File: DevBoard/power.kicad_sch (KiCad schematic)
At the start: 31 parts, among them U201 INA190A5IDDFR, U202 INA190A1IDDFR, U203 TPS70950DBVR, U204 TPS62177DQCR

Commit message: Dev board: cost-down pass (about $113 -> $80 per board at 5 boards)
Swaps from docs/devboard/cost-down-2026-10-14.md, datasheet-checked:
- L401/L501 XAL7030 -> SMMS1040-2R2M (Isat 18 A, Irms 12 A, 9 mOhm)
- L402/L502 SRP5030T -> APS0530M3R3H (new footprint L_Coilank_APS0530)
- L201 SRN4018TA -> FNR4030S100MT
- U203 TPS70950 -> HT7550-1, C204/C205 10 uF per Holtek's basic circuit
- C431/C434/C435 47 uF 1210 -> 22 uF 1206 (bank ~114 uF effective)
- JLC basic/preferred equivalents: D103, D401, R410/R412, C105/C206,
  C406, Q103 -> AO3400A
- D301 (out of stock) -> red KT-0603R
- R431/R531 -> bridged solder jumper
- 34 test loops -> bare pads; pin headers hand-soldered
- U301 bought from ST and consigned to JLC

ERC unchanged (0 errors, 8 expected GPIO-to-GND warnings).

Co-Authored-By: Claude Opus 5.5 <noreply@anthropic.com>
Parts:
- C204: value 1u 50V -> 10u 50V; footprint Capacitor_SMD:C_0805_2012Metric -> Capacitor_SMD:C_1206_3216Metric; LCSC C28323 -> C13585; MPN CL21B105KBFNNNE -> CL31A106KBHNNNE; Notes (none) -> HT7550 input: Holtek basic circuit 10 uF; 50 V and more C d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
- C205: value 4.7u 25V -> 10u 25V; LCSC C1779 -> C15850; MPN CL21A475KAQNNNE -> CL21A106KAYNNNE; Notes TPS709 needs >= 1.5 uF effective at 5 V (review m3) -> HT7550 output: Holtek basic circuit 10 uF (was 4.7 uF for t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
- C206: footprint Capacitor_SMD:C_0805_2012Metric -> Capacitor_SMD:C_1206_3216Metric; LCSC C2762602 -> C50254; MPN CL21B225KBYNNNE -> CL31B225KBHNNNE
- JP201, JP202: LCSC C492401 -> (none); Sourcing (none) -> Hand-solder, not JLC assembled (through-hole; LCSC C492401 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
- L201: footprint Inductor_SMD:L_Bourns-SRN4018 -> Inductor_SMD:L_Changjiang_FNR4030S; LCSC C2044417 -> C167879; MPN SRN4018TA-100M -> FNR4030S100MT (Changjiang); Notes (none) -> 10 uH as in the TPS62177 datasheet application (LPS4018-103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
- TP204, TP205: footprint MonolithDev:TestPoint_Harwin_S2761_0603 -> TestPoint:TestPoint_Pad_D1.5mm; LCSC C55121754 -> (none); MPN RH-S2761-46R (ronghe; Harwin S2761-46R equivalent) -> (none); now left out of the parts list
- U203: value TPS70950DBVR -> HT7550-1; footprint Package_TO_SOT_SMD:SOT-23-5 -> Package_TO_SOT_SMD:SOT-89-3; symbol MonolithDev:TPS70950DBV -> Regulator_Linear:HT75xx-1-SOT89; LCSC C96028 -> C16106; MPN (none) -> HT7550-1 (Holtek); Notes (none) -> Cost-down 2026-10-14 (was TPS70950DBVR): JLC preferred. Sup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
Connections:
- net 5V_AMP: now also U203.3 (VOUT); no longer U203.5 (OUT)
- net GND: now also U203.1 (GND); no longer U203.2 (GND)
- net LDO_IN: now also U203.2 (VIN); no longer U203.1 (IN)
- no-connect marks 4 -> 2
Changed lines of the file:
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@@
 		(rev "A (draft)")
 		(company "Monolith 100 W battery bank - dev board")
-		(comment 1 "R_MEAS + INA190 x2, TPS70950, TPS62177")
+		(comment 1 "R_MEAS + INA190 x2, HT7550-1, TPS62177")
 		(comment 2 "Spec + open items: DevBoard/README.md")
 		(comment 3 "Not reviewed, laid out, built or tested")
@@
 	)
 	(no_connect
-		(at 97.79 232.41)
-	)
-	(no_connect
 		(at 118.11 185.42)
 	)
-	(no_connect
-		(at 80.01 232.41)
-	)
 	(wire
 		(pts
@@
 			)
 		)
-		(property "Value" "1u 50V"
+		(property "Value" "10u 50V"
 			(at 75.03 234.51 0)
 			(show_name no)
@@
 			)
 		)
-		(property "Footprint" "Capacitor_SMD:C_0805_2012Metric"
+		(property "Footprint" "Capacitor_SMD:C_1206_3216Metric"
 			(at 69.545 229.87 0)
 			(hide yes)
@@
 			)
 		)
+		(property "Notes" "HT7550 input: Holtek basic circuit 10 uF; 50 V and more C damp the JP202 hot-plug ring"
+			(at 68.58 233.68 0)
+			(hide yes)
+			(show_name no)
+			(do_not_autoplace no)
+			(effects
+				(font
+					(size 1.27 1.27)
+				)
+			)
+		)
 		(property "Description" "Unpolarized capacitor"
 			(at 68.58 233.68 0)
@@
 			)
 		)
-		(property "LCSC" "C28323"
+		(property "LCSC" "C13585"
 			(at 68.58 233.68 0)
 			(hide yes)
@@
 			)
 		)
-		(property "MPN" "CL21B105KBFNNNE"
+		(property "MPN" "CL31A106KBHNNNE"
 			(at 68.58 233.68 0)
 			(hide yes)
@@
 			)
 		)
-		(property "Value" "4.7u 25V"
+		(property "Value" "10u 25V"
 			(at 114.34 234.51 0)
 			(show_name no)
@@
 			)
 		)
-		(property "LCSC" "C1779"
+		(property "LCSC" "C15850"
 			(at 106.68 233.68 0)
 			(hide yes)
@@
 			)
 		)
-		(property "MPN" "CL21A475KAQNNNE"
+		(property "MPN" "CL21A106KAYNNNE"
 			(at 106.68 233.68 0)
 			(hide yes)
@@
 			)
 		)
-		(property "Notes" "TPS709 needs >= 1.5 uF effective at 5 V (review m3)"
+		(property "Notes" "HT7550 output: Holtek basic circuit 10 uF (was 4.7 uF for the TPS709, review m3)"
 			(at 106.68 233.68 0)
 			(hide yes)
@@
 			)
 		)
-		(property "Footprint" "Capacitor_SMD:C_0805_2012Metric"
+		(property "Footprint" "Capacitor_SMD:C_1206_3216Metric"
 			(at 122.885 59.69 0)
 			(hide yes)
@@
 			)
 		)
-		(property "LCSC" "C2762602"
+		(property "LCSC" "C50254"
 			(at 121.92 63.5 0)
 			(hide yes)
@@
 			)
 		)
-		(property "MPN" "CL21B225KBYNNNE"
+		(property "MPN" "CL31B225KBHNNNE"
 			(at 121.92 63.5 0)
 			(hide yes)
@@
 		(body_style 1)
 		(exclude_from_sim no)
-		(in_bom yes)
+		(in_bom no)
 		(on_board yes)
 		(in_pos_files yes)
@@
 			)
 		)
-		(property "Footprint" "MonolithDev:TestPoint_Harwin_S2761_0603"
+		(property "Footprint" "TestPoint:TestPoint_Pad_D1.5mm"
 			(at 132.08 68.58 0)
 			(hide yes)
@@
 			)
 		)
-		(property "LCSC" "C55121754"
-			(at 127 68.58 0)
-			(hide yes)
-			(show_name no)
-			(do_not_autoplace no)
-			(effects
-				(font
-					(size 1.27 1.27)
-				)
-			)
-		)
-		(property "MPN" "RH-S2761-46R (ronghe; Harwin S2761-46R equivalent)"
-			(at 127 68.58 0)
-			(hide yes)
-			(show_name no)
-			(do_not_autoplace no)
-			(effects
-				(font
-					(size 1.27 1.27)
-				)
-			)
-		)
 		(pin "1"
 		)
@@
 		(body_style 1)
 		(exclude_from_sim no)
-		(in_bom yes)
+		(in_bom no)
 		(on_board yes)
 		(in_pos_files yes)
@@
 			)
 		)
-		(property "Footprint" "MonolithDev:TestPoint_Harwin_S2761_0603"
+		(property "Footprint" "TestPoint:TestPoint_Pad_D1.5mm"
 			(at 111.76 55.88 0)
 			(hide yes)
@@
 			)
 		)
-		(property "LCSC" "C55121754"
-			(at 106.68 55.88 0)
-			(hide yes)
-			(show_name no)
-			(do_not_autoplace no)
-			(effects
-				(font
-					(size 1.27 1.27)
-				)
-			)
-		)
-		(property "MPN" "RH-S2761-46R (ronghe; Harwin S2761-46R equivalent)"
-			(at 106.68 55.88 0)
-			(hide yes)
-			(show_name no)
-			(do_not_autoplace no)
-			(effects
-				(font
-					(size 1.27 1.27)
-				)
-			)
-		)
 		(pin "1"
 		)
@@
 		(in_bom yes)
 		(on_board yes)
-		(in_pos_files yes)
+		(in_pos_files no)
 		(dnp no)
 		(property "Reference" "JP202"
@@
 			)
 		)
-		(property "Description" "Jumper, 2-pole, open"
+		(property "Sourcing" "Hand-solder, not JLC assembled (through-hole; LCSC C492401 PZ254V-11-02P)"
 			(at 50.8 229.87 0)
 			(hide yes)
@@
 			)
 		)
-		(property "LCSC" "C492401"
+		(property "Description" "Jumper, 2-pole, open"
 			(at 50.8 229.87 0)
 			(hide yes)
@@
 	)
 	(symbol
-		(lib_id "MonolithDev:TPS70950DBV")
-		(at 88.9 231.14 0)
+		(lib_id "Regulator_Linear:HT75xx-1-SOT89")
+		(at 88.90 232.41 0)
 		(unit 1)
 		(body_style 1)
@@
 			)
 		)
-		(property "Value" "TPS70950DBVR"
+		(property "Value" "HT7550-1"
 			(at 88.9 225.55 0)
 			(show_name no)
@@
 			)
 		)
-		(property "Footprint" "Package_TO_SOT_SMD:SOT-23-5"
+		(property "Footprint" "Package_TO_SOT_SMD:SOT-89-3"
 			(at 88.9 231.14 0)
 			(hide yes)
@@
 			)
 		)
-		(property "Datasheet" "https://www.ti.com/lit/ds/symlink/tps709.pdf"
+		(property "Datasheet" "https://www.farnell.com/datasheets/2047678.pdf"
 			(at 88.9 231.14 0)
 			(hide yes)
@@
 			)
 		)
-		(property "Description" "5.0 V 150 mA 1 uA Iq LDO"
+		(property "Notes" "Cost-down 2026-10-14 (was TPS70950DBVR): JLC preferred. Supplies only the two INA190s. +/-3 %, 30 V max input: the JP202 hot-plug ring (review 2 C-3, 23-30 V) is why C204 is 10 uF 50 V. Holtek basic circuit: 10 uF in and out. No EN pin (the TPS709 EN was left open)"
 			(at 88.9 231.14 0)
 			(hide yes)
@@
 			)
 		)
-		(property "LCSC" "C96028"
+		(property "MPN" "HT7550-1 (Holtek)"
+			(at 88.9 231.14 0)
+			(hide yes)
+			(show_name no)
+			(do_not_autoplace no)
+			(effects
+				(font
+					(size 1.27 1.27)
+				)
+			)
+		)
+		(property "Description" "Holtek HT7550-1 5 V LDO, 30 V input, 2.5 uA Iq, SOT-89 (1 GND, 2 VIN, 3 VOUT)"
+			(at 88.9 231.14 0)
+			(hide yes)
+			(show_name no)
+			(do_not_autoplace no)
+			(effects
+				(font
+					(size 1.27 1.27)
+				)
+			)
+		)
+		(property "LCSC" "C16106"
 			(at 88.9 231.14 0)
 			(hide yes)
@@
 		(pin "3"
 		)
-		(pin "4"
-		)
-		(pin "5"
-		)
 		(instances
 			(project "MonolithDev"
@@
 		(in_bom yes)
 		(on_board yes)
-		(in_pos_files yes)
+		(in_pos_files no)
 		(dnp no)
 		(property "Reference" "JP201"
@@
 			)
 		)
-		(property "Description" "Jumper, 2-pole, open"
+		(property "Sourcing" "Hand-solder, not JLC assembled (through-hole; LCSC C492401 PZ254V-11-02P)"
 			(at 132.08 229.87 0)
 			(hide yes)
@@
 			)
 		)
-		(property "Notes" "pull = amps off. Needs a 2.54 mm shunt (hand, not in the JLC BOM)"
-			(at 0 0 0)
+		(property "Description" "Jumper, 2-pole, open"
+			(at 132.08 229.87 0)
 			(hide yes)
 			(show_name no)
@@
 			)
 		)
-		(property "LCSC" "C492401"
-			(at 132.08 229.87 0)
+		(property "Notes" "pull = amps off. Needs a 2.54 mm shunt (hand, not in the JLC BOM)"
+			(at 0 0 0)
 			(hide yes)
 			(show_name no)
@@
 			)
 		)
-		(property "Footprint" "Inductor_SMD:L_Bourns-SRN4018"
+		(property "Footprint" "Inductor_SMD:L_Changjiang_FNR4030S"
 			(at 175.26 55.88 0)
 			(hide yes)
@@
 			)
 		)
+		(property "Notes" "10 uH as in the TPS62177 datasheet application (LPS4018-103); 130 mOhm, 1.6 A Irms / 2.4 A Isat for a 0.5 A converter. Cost-down 2026-10-14 (was SRN4018TA-100M)"
+			(at 175.26 55.88 0)
+			(hide yes)
+			(show_name no)
+			(do_not_autoplace no)
+			(effects
+				(font
+					(size 1.27 1.27)
+				)
+			)
+		)
 		(property "Description" "Inductor"
 			(at 175.26 55.88 0)
@@
 			)
 		)
-		(property "LCSC" "C2044417"
+		(property "LCSC" "C167879"
 			(at 175.26 55.88 0)
 			(hide yes)
@@
 			)
 		)
-		(property "MPN" "SRN4018TA-100M"
+		(property "MPN" "FNR4030S100MT (Changjiang)"
 			(at 175.26 55.88 0)
 			(hide yes)
@@
 		)
 	)
+	(wire
+		(pts
+			(xy 80.01 229.87) (xy 81.28 229.87)
+		)
+		(stroke
+			(width 0)
+			(type default)
+		)
+	)
+	(wire
+		(pts
+			(xy 96.52 229.87) (xy 97.79 229.87)
+		)
+		(stroke
+			(width 0)
+			(type default)
+		)
+	)

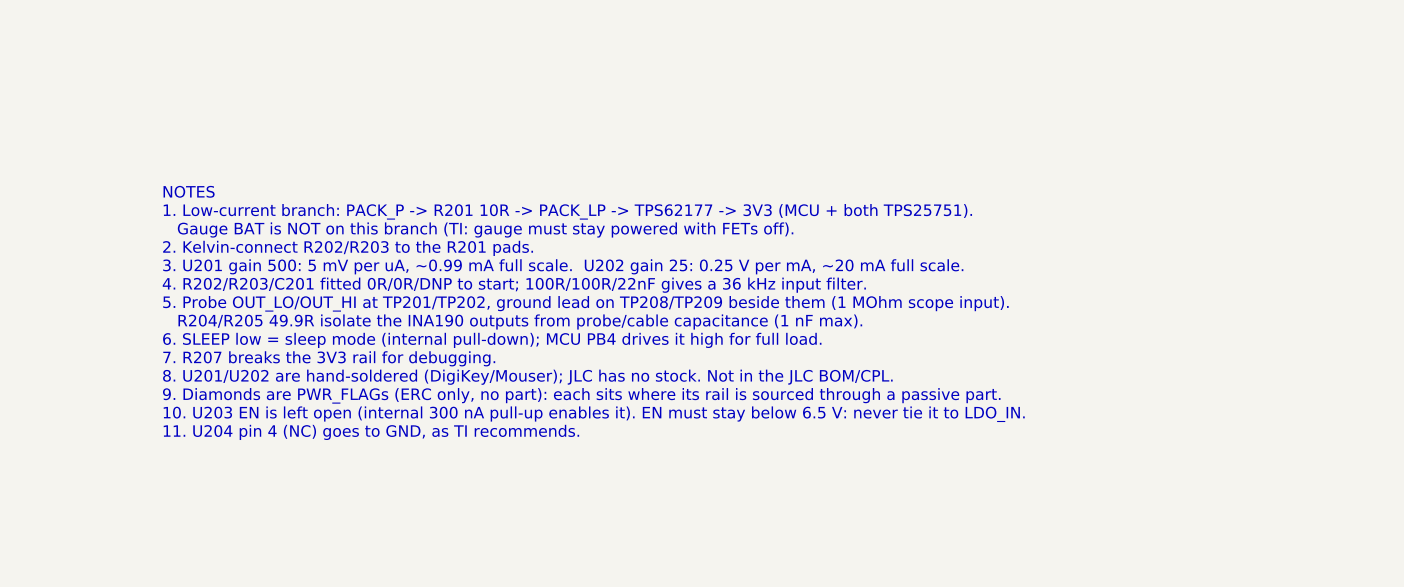
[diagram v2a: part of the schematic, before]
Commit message: Dev board rev A8 part 2: review 4 docs, BOM, A-2 procedure, J104 clamp
Schematic edits by tools/review4_docs.py (helpers split out of
review4_fixes.py into tools/sch_edit.py; review4_fixes output unchanged).
- A-2: EV2400 work only with 3V3 up (J104) and U301 in reset; checklist,
  R312/R301 Notes and MCU sheet note 10 rewritten.
- D-5: D105 SMAJ18A clamp on the J104 side of D104; board placed
  (D104 moved one body width left).
- Stale Notes, sheet notes, heading and address text fixed; sheet 4
  renamed "MCU and Sensors"; revision log A7/A8; title blocks A8.
- MPNs filled on the parts that had only LCSC numbers; Sourcing on U301
  and J301; J301 out of the position file.
- bringup-config-checklist, mcu-io-power-states and power-budget rewritten
  for the CC2340 with every review 4 CONFIG item; corrections in
  circuit-description, cost-down and cc2340-pin-budget.
ERC: 8 known warnings. 0 text overlaps. DRC: 0 parity issues, no
courtyard overlaps (429 parts). README item 42.

Co-Authored-By: Claude Opus 5.5 <noreply@anthropic.com>
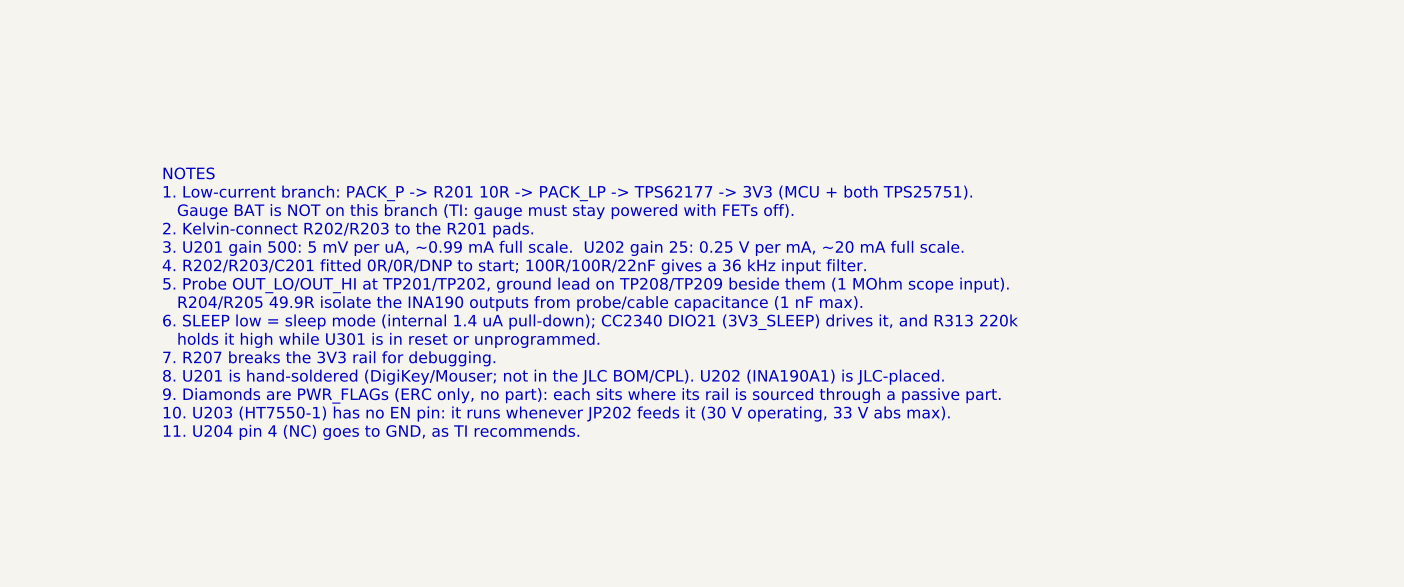
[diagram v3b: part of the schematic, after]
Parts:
- U204: MPN (none) -> TPS62177DQCR
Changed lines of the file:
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@@
 		(title "Sleep-current measurement and 3.3 V rail")
 		(date "2026-10-14")
-		(rev "A6")
+		(rev "A8")
 		(company "Monolith 100 W battery bank - dev board")
 		(comment 1 "R_MEAS + INA190 x2, HT7550-1, TPS62177")
@@
 		)
 	)
-	(text "NOTES\n1. Low-current branch: PACK_P -> R201 10R -> PACK_LP -> TPS62177 -> 3V3 (MCU + both TPS25751).\n   Gauge BAT is NOT on this branch (TI: gauge must stay powered with FETs off).\n2. Kelvin-connect R202/R203 to the R201 pads.\n3. U201 gain 500: 5 mV per uA, ~0.99 mA full scale.  U202 gain 25: 0.25 V per mA, ~20 mA full scale.\n4. R202/R203/C201 fitted 0R/0R/DNP to start; 100R/100R/22nF gives a 36 kHz input filter.\n5. Probe OUT_LO/OUT_HI at TP201/TP202, ground lead on TP208/TP209 beside them (1 MOhm scope input).\n   R204/R205 49.9R isolate the INA190 outputs from probe/cable capacitance (1 nF max).\n6. SLEEP low = sleep mode (internal pull-down); MCU PB4 drives it high for full load.\n7. R207 breaks the 3V3 rail for debugging.\n8. U201/U202 are hand-soldered (DigiKey/Mouser); JLC has no stock. Not in the JLC BOM/CPL.\n9. Diamonds are PWR_FLAGs (ERC only, no part): each sits where its rail is sourced through a passive part.\n10. U203 EN is left open (internal 300 nA pull-up enables it). EN must stay below 6.5 V: never tie it to LDO_IN.\n11. U204 pin 4 (NC) goes to GND, as TI recommends."
+	(text "NOTES\n1. Low-current branch: PACK_P -> R201 10R -> PACK_LP -> TPS62177 -> 3V3 (MCU + both TPS25751).\n   Gauge BAT is NOT on this branch (TI: gauge must stay powered with FETs off).\n2. Kelvin-connect R202/R203 to the R201 pads.\n3. U201 gain 500: 5 mV per uA, ~0.99 mA full scale.  U202 gain 25: 0.25 V per mA, ~20 mA full scale.\n4. R202/R203/C201 fitted 0R/0R/DNP to start; 100R/100R/22nF gives a 36 kHz input filter.\n5. Probe OUT_LO/OUT_HI at TP201/TP202, ground lead on TP208/TP209 beside them (1 MOhm scope input).\n   R204/R205 49.9R isolate the INA190 outputs from probe/cable capacitance (1 nF max).\n6. SLEEP low = sleep mode (internal 1.4 uA pull-down); CC2340 DIO21 (3V3_SLEEP) drives it, and R313 220k\n   holds it high while U301 is in reset or unprogrammed.\n7. R207 breaks the 3V3 rail for debugging.\n8. U201 is hand-soldered (DigiKey/Mouser; not in the JLC BOM/CPL). U202 (INA190A1) is JLC-placed.\n9. Diamonds are PWR_FLAGs (ERC only, no part): each sits where its rail is sourced through a passive part.\n10. U203 (HT7550-1) has no EN pin: it runs whenever JP202 feeds it (30 V operating, 33 V abs max).\n11. U204 pin 4 (NC) goes to GND, as TI recommends."
 		(exclude_from_sim no)
 		(at 215.9 129.54 0)
@@
 			(at 152.4 63.5 0)
 			(hide yes)
+			(show_name no)
+			(do_not_autoplace no)
+			(effects
+				(font
+					(size 1.27 1.27)
+				)
+			)
+		)
+		(property "MPN" "TPS62177DQCR"
+			(at 152.4 63.5 0)
+			(hide yes)
